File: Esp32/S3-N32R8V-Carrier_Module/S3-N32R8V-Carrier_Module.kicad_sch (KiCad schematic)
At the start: 1 part, among them U101 ESP32-S3-WROOM-2

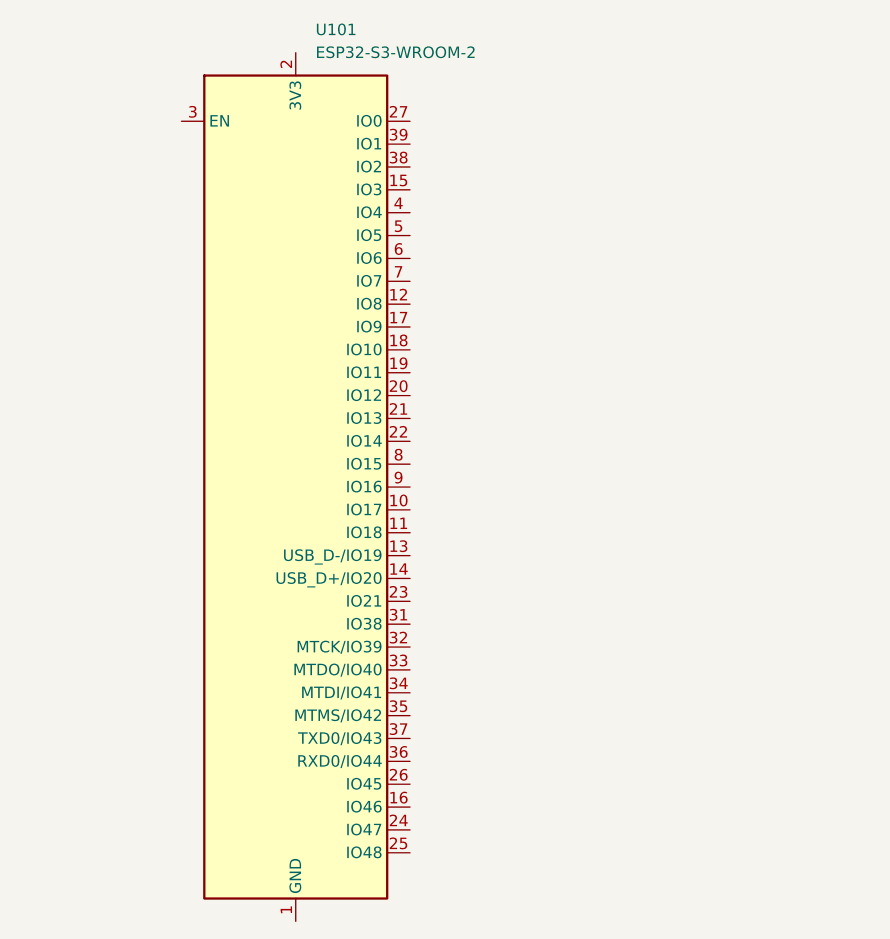
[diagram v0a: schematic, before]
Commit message: Carrier Board
Added Carrier board for the ESP32-XIAO  Board
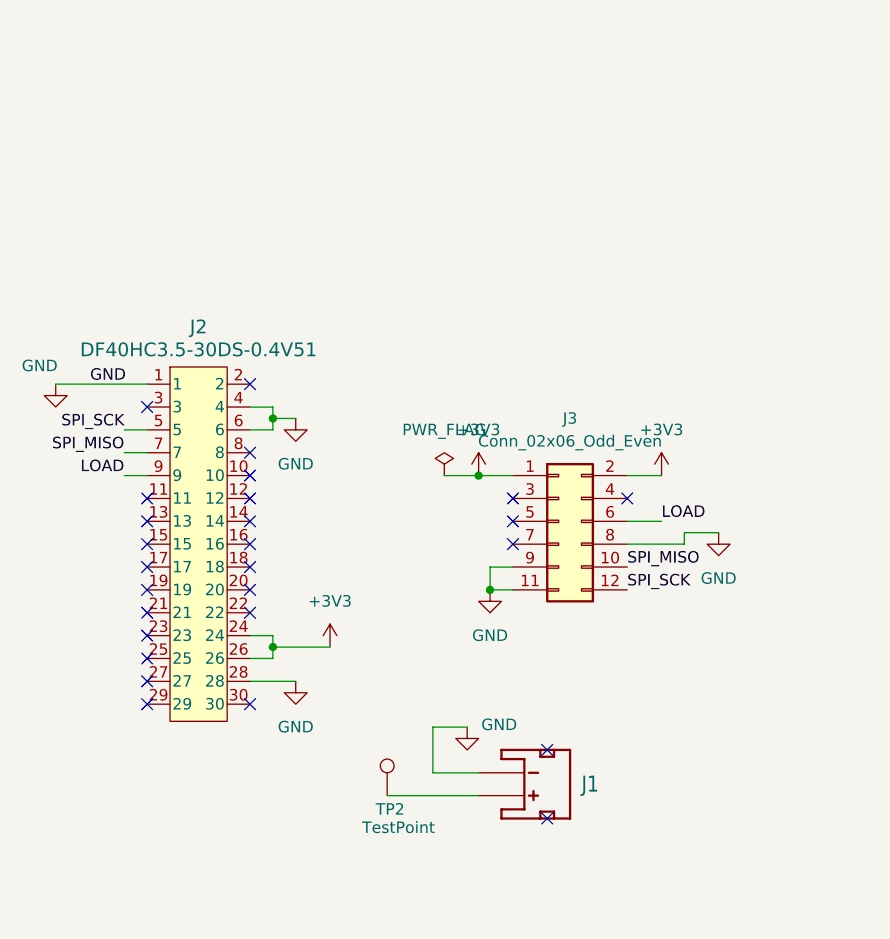
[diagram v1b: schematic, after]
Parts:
- removed U101: ESP32-S3-WROOM-2, RF_Module:ESP32-S3-WROOM-2, symbol RF_Module:ESP32-S3-WROOM-2
- added J1: ~, Connector_JST:JST_PH_S2B-PH-SM4-TB_1x02-1MP_P2.00mm_Horizontal, symbol SparkFun-Connectors:JST_2MM_MALE
- added J2: DF40HC3.5-30DS-0.4V51, con-hirose-df40:CONN_DF40HC3.5-30DS-0.4V51_HIR, symbol con-hirose-df40:DF40HC3.5-30DS-0.4V51
- added J3: Conn_02x06_Odd_Even, Connector_PinHeader_2.54mm:PinHeader_2x06_P2.54mm_Vertical_SMD, symbol Connector_Generic:Conn_02x06_Odd_Even
- added TP2: TestPoint, TestPoint:TestPoint_Pad_1.0x1.0mm, symbol Connector:TestPoint
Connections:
- new net: J1.2 (+), TP2.1
- new net +3V3: J2.24, J2.26, J3.1 (Pin_1), J3.2 (Pin_2)
- new net GND: J1.1 (-), J2.1, J2.28, J2.4, J2.6, J3.11 (Pin_11), J3.8 (Pin_8), J3.9 (Pin_9)
- new net LOAD: J2.9, J3.6 (Pin_6)
- new net SPI_MISO: J2.7, J3.10 (Pin_10)
- new net SPI_SCK: J2.5, J3.12 (Pin_12)
- no-connect marks 0 -> 27

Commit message: Connector
Modify jst connector (Need to look for the correct One)
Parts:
- added H101: MountingHole, MountingHole:MountingHole_2.7mm, symbol Mechanical:MountingHole
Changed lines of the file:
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@@
+	)
+	(symbol
+		(lib_id "Mechanical:MountingHole")
+		(at 182.88 120.65 0)
+		(unit 1)
+		(exclude_from_sim yes)
+		(in_bom no)
+		(on_board yes)
+		(dnp no)
+		(fields_autoplaced yes)
+		(property "Reference" "H101"
+			(at 185.42 119.3799 0)
+			(effects
+				(font
+					(size 1.27 1.27)
+				)
+				(justify left)
+			)
+		)
+		(property "Value" "MountingHole"
+			(at 185.42 121.9199 0)
+			(effects
+				(font
+					(size 1.27 1.27)
+				)
+				(justify left)
+			)
+		)
+		(property "Footprint" "MountingHole:MountingHole_2.7mm"
+			(at 182.88 120.65 0)
+			(effects
+				(font
+					(size 1.27 1.27)
+				)
+				(hide yes)
+			)
+		)
+		(property "Datasheet" "~"
+			(at 182.88 120.65 0)
+			(effects
+				(font
+					(size 1.27 1.27)
+				)
+				(hide yes)
+			)
+		)
+		(property "Description" "Mounting Hole without connection"
+			(at 182.88 120.65 0)
+			(effects
+				(font
+					(size 1.27 1.27)
+				)
+				(hide yes)
+			)
+		)
+		(instances
+			(project ""
+				(path "/04a6d993-4a0c-40c5-bc8c-e5d33aed3dbd"
+					(reference "H101")
+					(unit 1)
+				)
+			)
+		)
 	)
 	(symbol
